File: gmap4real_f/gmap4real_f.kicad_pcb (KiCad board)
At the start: 2 copper layers, 24.1 x 53.3 mm, 8 parts

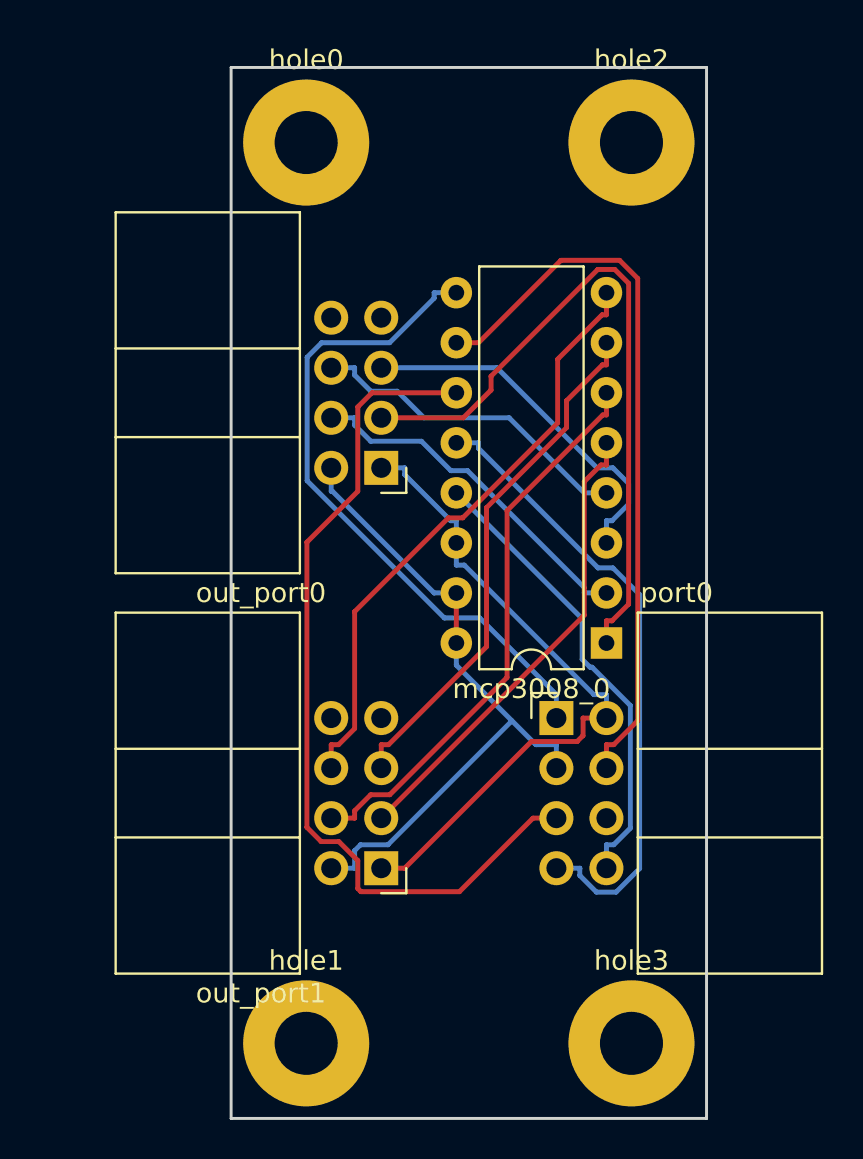
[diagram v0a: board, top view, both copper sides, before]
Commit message: smaller PCBs
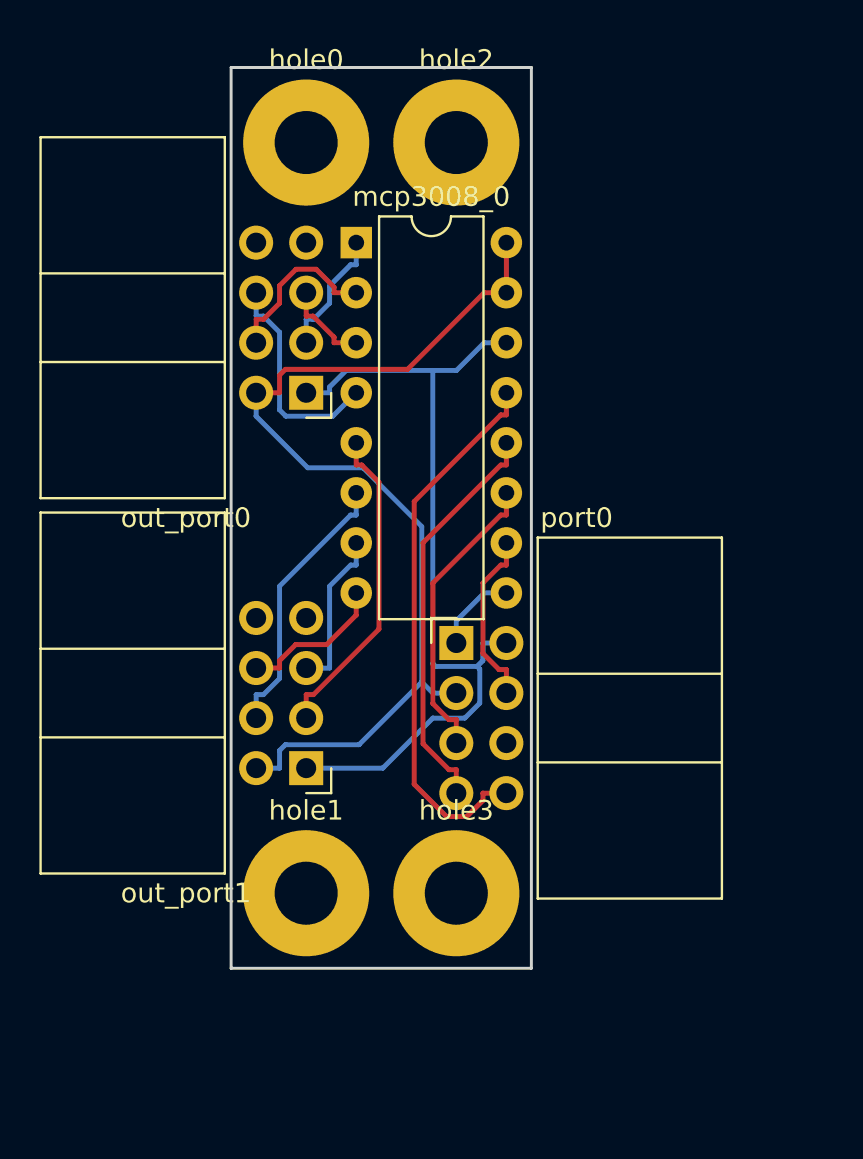
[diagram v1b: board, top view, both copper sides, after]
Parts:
- moved mcp3008_0 24.0 mm to (165.1, 44.5), turned to 0 degrees
- moved hole3 11.7 mm to (170.2, 77.5)
- moved hole2 8.89 mm to (170.2, 39.4)
- moved hole1 7.62 mm to (162.6, 77.5)
- moved out_port1 6.35 mm to (162.6, 71.1)
- moved port0 6.35 mm to (170.2, 64.8)
- moved out_port0 5.39 mm to (162.6, 52.1)
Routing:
- net gnd: track 33.7 -> 4.29 mm
- net mosi: track 44.1 -> 15.1 mm
- net slider0: track 35.3 -> 6.51 mm
- net cs3008: track 37.0 -> 8.99 mm
- net slider7: track 30.7 -> 7.54 mm
- net slider6: track 26.7 -> 8.26 mm
- net 3.3v: track 34.1 -> 50.4 mm
- net slider5: track 28.7 -> 13.9 mm
- net slider2: track 18.6 -> 4.45 mm
- net miso: track 32.0 -> 20.6 mm
- net slider1: track 18.0 -> 8.50 mm
- net agnd: track 34.0 -> 43.2 mm
- net slider4: track 23.9 -> 16.4 mm
- net slider3: track 16.8 -> 11.2 mm
- net sck: track 23.5 -> 28.0 mm
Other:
- board size 24.1 x 53.3 mm -> 15.2 x 45.7 mm
